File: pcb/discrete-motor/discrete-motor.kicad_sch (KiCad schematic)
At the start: 28 parts, among them J1 ScrewTerminal, U1 PinHeader8, U2 PinHeader8

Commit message: wip
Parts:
- removed CCLFCUR1: (no value), Capacitor_SMD:C_0603_1608Metric, symbol Device:C
- removed RCLFCUR1, RCLPCUR1, RCLSCUR1: (no value), Resistor_SMD:R_0603_1608Metric, symbol Device:R
- removed UCLCUR1: (no value), Package_SO:SOIC-5, symbol Comparator:LMV331
- added CF10, CSA10: 100n, Capacitor_SMD:C_0603_1608Metric, symbol Device:C
- added R10: 10m, Resistor_SMD:R_1206_3216Metric, symbol Device:R
- added RF10: 1k, Resistor_SMD:R_0603_1608Metric, symbol Device:R
- added UA10: (no value), Package_TO_SOT_SMD:SOT-23-6, symbol Amplifier_Current:INA181
- C10: value (none) -> 100n
- J1: value ScrewTerminal -> (none)
- QH10, QL10: footprint Package_TO_SOT_THT:TO-263-2 -> fixme!!!
- R1: value (none) -> 4.7k
- R4: value (none) -> 330
- RH10, RL10: value (none) -> 10
- U1, U2: value PinHeader8 -> (none)
- U3, U4: value ~ -> (none)
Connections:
- net 3V3: now also CSA10.1, UA10.5 (REF)
- net GND: now also CF10.2, CSA10.2, R10.2, UA10.2 (GND), UA10.4 (-), UA10.6 (V+)
- net at U10.3 (~{SD}): now also U1.7 (Pin_7)
- net at U2.2 (Pin_2): now also CF10.1, RF10.2
- net at J4.1 (Pin_1): now also C10.2, QH10.3 (S), QL10.2 (D), U10.6 (VS)
- net at QL10.3 (S): now also R10.1, UA10.3 (+)
- new net: RF10.1, UA10.1
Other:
- moved on the sheet: C10, D10, QH10, QL10, RH10, RL10, U10

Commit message: wip
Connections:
- net at U1.7 (Pin_7): no longer U10.3 (~{SD})
- net at U1.8 (Pin_8): now also U10.3 (~{SD})

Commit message: discrete motor
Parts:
- removed R10: 10m, Resistor_SMD:R_1206_3216Metric, symbol Device:R
- added C11, C12, C13, CF11, CSA11: 100n, Capacitor_SMD:C_0603_1608Metric, symbol Device:C
- added D11, D12, D13: ~, Diode_SMD:D_SMA, symbol Device:D
- added QH11, QH12, QH13, QL11, QL12, QL13: ~, Package_TO_SOT_SMD:TO-263-2, symbol Transistor_FET:Q_NMOS_GDS
- added RF11: 1k, Resistor_SMD:R_0603_1608Metric, symbol Device:R
- added RH11, RH12, RH13, RL11, RL12, RL13: 10, Resistor_SMD:R_0603_1608Metric, symbol Device:R
- added RS10, RS11: 10m, Resistor_SMD:R_1206_3216Metric, symbol Device:R
- added U11, U12, U13: ~, Package_SO:SOIC-8_3.9x4.9mm_P1.27mm, symbol Driver_FET:IR2104
- added UA11: ~, Package_TO_SOT_SMD:SOT-23-6, symbol Amplifier_Current:INA181
- D1, D10, J1, J2, J3, J4, J5, U1, U2, U3, U4, U5, U6, U7, U8, UA10: value (none) -> ~
- QH10, QL10: value (none) -> ~; footprint fixme!!! -> Package_TO_SOT_SMD:TO-263-2; lcsc (none) -> C409762
- U10: value (none) -> ~; footprint Package_SO:SOIC-8 -> Package_SO:SOIC-8_3.9x4.9mm_P1.27mm; lcsc (none) -> C5804631
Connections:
- net 12V: now also D11.2 (A), D12.2 (A), D13.2 (A), QH11.2 (D), QH12.2 (D), QH13.2 (D), U11.1 (VCC), U12.1 (VCC), U13.1 (VCC)
- net 3V3: now also CSA11.1, UA11.5 (REF)
- net GND: now also CF11.2, CSA11.2, RS10.2, RS11.2, U11.4 (COM), U12.4 (COM), U13.4 (COM), UA11.2 (GND), UA11.4 (-), UA11.6 (V+)
- net at U2.1 (Pin_1): no longer U10.2 (IN)
- net at U2.4 (Pin_4): now also CF11.1, RF11.2
- net at J4.2 (Pin_2): now also C11.2, QH11.3 (S), QL11.2 (D), U11.6 (VS)
- net at J4.3 (Pin_3): now also C12.2, QH12.3 (S), QL12.2 (D), U12.6 (VS)
- net at J4.4 (Pin_4): now also C13.2, QH13.3 (S), QL13.2 (D), U13.6 (VS)
- net at QL10.3 (S), UA10.3 (+): now also QL11.3 (S), RS10.1
- net at U1.2 (Pin_2): now also U10.2 (IN)
- net at U1.3 (Pin_3): now also U11.2 (IN)
- net at U1.6 (Pin_6): now also U12.2 (IN)
- net at U1.7 (Pin_7): now also U13.2 (IN)
- net at U1.8 (Pin_8), U10.3 (~{SD}): now also U11.3 (~{SD}), U12.3 (~{SD}), U13.3 (~{SD})
- new net: C12.1, D12.1 (K), U12.8 (VB)
- new net: C13.1, D13.1 (K), U13.8 (VB)
- new net: QL11.1 (G), RL11.2
- new net: C11.1, D11.1 (K), U11.8 (VB)
- new net: QL12.1 (G), RL12.2
- new net: QL12.3 (S), QL13.3 (S), RS11.1, UA11.3 (+)
- new net: RL11.1, U11.5 (LO)
- new net: RH11.1, U11.7 (HO)
- new net: RL13.1, U13.5 (LO)
- new net: RH13.1, U13.7 (HO)
- new net: QH13.1 (G), RH13.2
- new net: RF11.1, UA11.1
- new net: QH11.1 (G), RH11.2
- new net: QL13.1 (G), RL13.2
- new net: QH12.1 (G), RH12.2
- new net: RL12.1, U12.5 (LO)
- new net: RH12.1, U12.7 (HO)

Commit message: pcb wip
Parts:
- C10, C11, C12, C13, CF10, CF11, CSA10, CSA11: lcsc C53084461 -> C1590
- D1, D10, D11, D12, D13, J1, J2, J3, J4, J5, U1, U2, U3, U4, U5, U6, U7, U8, UA10, UA11: value ~ -> (none)
- QH10, QH11, QH12, QH13, QL10, QL11, QL12, QL13: value ~ -> (none); lcscRot (none) -> 180
- RH10, RH11, RH12, RH13, RL10, RL11, RL12, RL13: footprint Resistor_SMD:R_0603_1608Metric -> Resistor_SMD:R_0402_1005Metric
- U10, U11, U12, U13: value ~ -> (none); lcscRot (none) -> -90

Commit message: wip
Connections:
- net 12V: no longer D10.2 (A), D11.2 (A), D12.2 (A), D13.2 (A), QH10.2 (D), QH11.2 (D), QH12.2 (D), QH13.2 (D), U10.1 (VCC), U11.1 (VCC), U12.1 (VCC), U13.1 (VCC)
- net GND: now also J2.1 (Pin_1)
- net VMOT: now reaches J2.2 (Pin_2)
- net VMOT: now also D10.2 (A), D11.2 (A), D12.2 (A), D13.2 (A), QH10.2 (D), QH11.2 (D), QH12.2 (D), QH13.2 (D), U10.1 (VCC), U11.1 (VCC), U12.1 (VCC), U13.1 (VCC)
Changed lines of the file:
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@@
     )
   )
-  (label "12V"
-    (at 76.2 119.38 180)
-    (effects
-      (font
-        (size 1.27 1.27)
-      )
-      (justify right bottom)
-    )
-  )
-  (label "12V"
-    (at 76.2 88.9 180)
-    (effects
-      (font
-        (size 1.27 1.27)
-      )
-      (justify right bottom)
-    )
-  )
   (label "GND"
     (at 76.2 83.82 180)
@@
     )
   )
-  (label "12V"
-    (at 107.95 60.96 180)
-    (effects
-      (font
-        (size 1.27 1.27)
-      )
-      (justify right bottom)
-    )
-  )
   (label "GND"
     (at 123.19 95.25 180)
@@
     )
   )
-  (label "12V"
-    (at 107.95 121.92 180)
-    (effects
-      (font
-        (size 1.27 1.27)
-      )
-      (justify right bottom)
-    )
-  )
   (label "3V3"
     (at 97.79 34.29 180)
@@
     )
   )
-  (label "12V"
-    (at 76.2 58.42 180)
-    (effects
-      (font
-        (size 1.27 1.27)
-      )
-      (justify right bottom)
-    )
-  )
   (label "GND"
     (at 133.35 140.97 180)
@@
     )
   )
-  (label "12V"
-    (at 76.2 149.86 180)
-    (effects
-      (font
-        (size 1.27 1.27)
-      )
-      (justify right bottom)
-    )
-  )
   (label "GND"
     (at 76.2 114.3 180)
@@
     )
   )
-  (label "12V"
-    (at 107.95 91.44 180)
-    (effects
-      (font
-        (size 1.27 1.27)
-      )
-      (justify right bottom)
-    )
-  )
   (label "5V"
     (at 97.79 29.21 180)
@@
     )
   )
-  (label "12V"
-    (at 107.95 152.4 180)
-    (effects
-      (font
-        (size 1.27 1.27)
-      )
-      (justify right bottom)
-    )
-  )
   (label "GND"
     (at 62.23 27.94 180)
@@
     )
   )
+  (label "GND"
+    (at 48.260000000000005 49.53 180)
+    (effects
+      (font
+        (size 1.27 1.27)
+      )
+      (justify right bottom)
+    )
+  )
+  (label "VMOT"
+    (at 48.260000000000005 52.07 180)
+    (effects
+      (font
+        (size 1.27 1.27)
+      )
+      (justify right bottom)
+    )
+  )
+  (label "VMOT"
+    (at 76.2 58.42 180)
+    (effects
+      (font
+        (size 1.27 1.27)
+      )
+      (justify right bottom)
+    )
+  )
+  (label "VMOT"
+    (at 107.95 60.96000000000001 180)
+    (effects
+      (font
+        (size 1.27 1.27)
+      )
+      (justify right bottom)
+    )
+  )
+  (label "VMOT"
+    (at 76.2 88.89999999999999 180)
+    (effects
+      (font
+        (size 1.27 1.27)
+      )
+      (justify right bottom)
+    )
+  )
+  (label "VMOT"
+    (at 107.95 91.44 180)
+    (effects
+      (font
+        (size 1.27 1.27)
+      )
+      (justify right bottom)
+    )
+  )
+  (label "VMOT"
+    (at 76.2 119.38000000000001 180)
+    (effects
+      (font
+        (size 1.27 1.27)
+      )
+      (justify right bottom)
+    )
+  )
+  (label "VMOT"
+    (at 107.95 121.92 180)
+    (effects
+      (font
+        (size 1.27 1.27)
+      )
+      (justify right bottom)
+    )
+  )
+  (label "VMOT"
+    (at 76.2 149.86 180)
+    (effects
+      (font
+        (size 1.27 1.27)
+      )
+      (justify right bottom)
+    )
+  )
+  (label "VMOT"
+    (at 107.95 152.39999999999998 180)
+    (effects
+      (font
+        (size 1.27 1.27)
+      )
+      (justify right bottom)
+    )
+  )

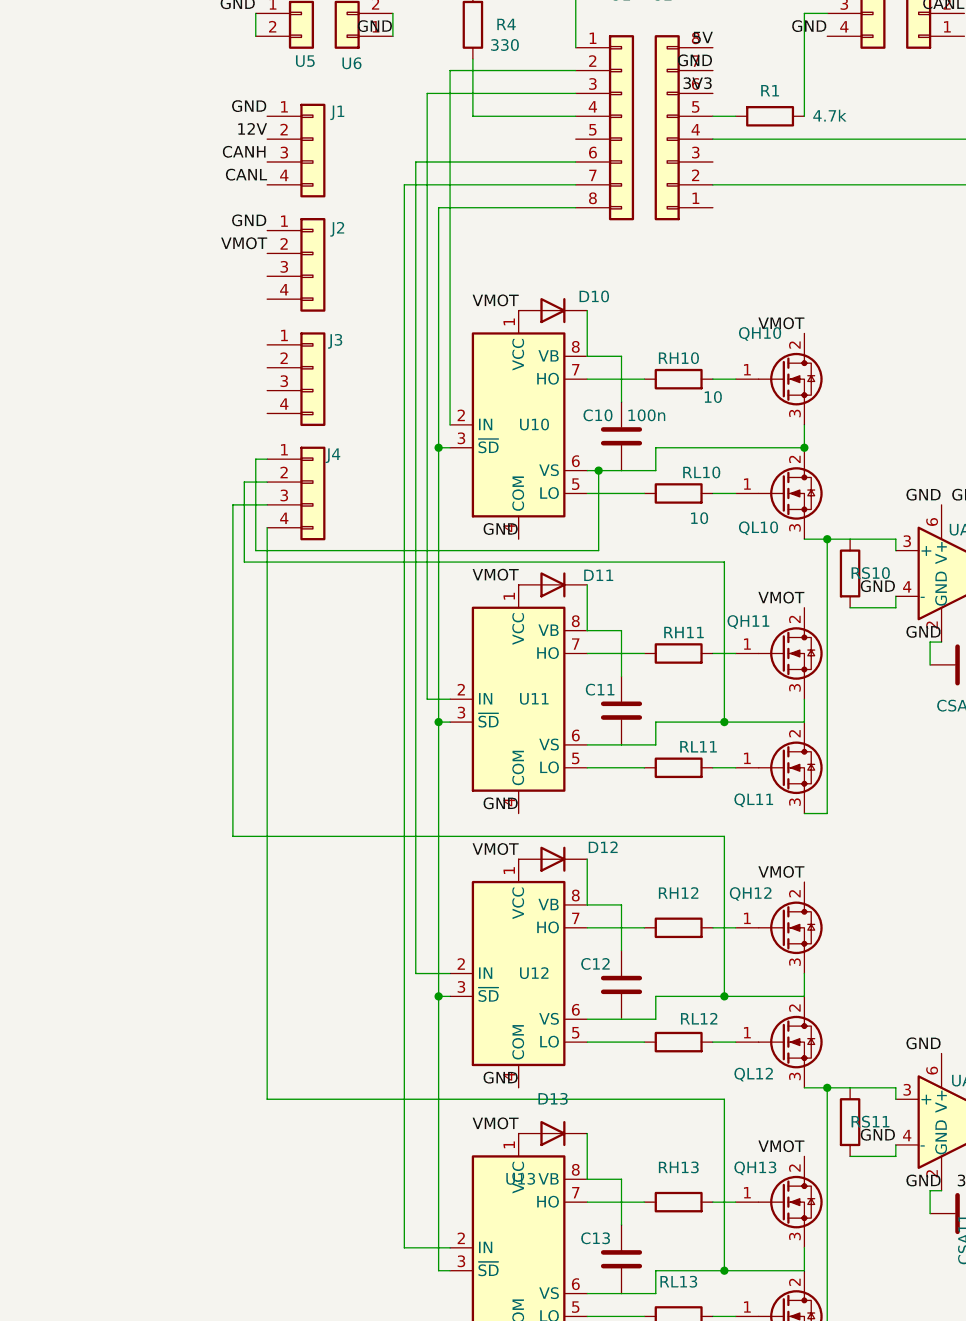
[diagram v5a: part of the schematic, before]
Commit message: discrete motor fixes
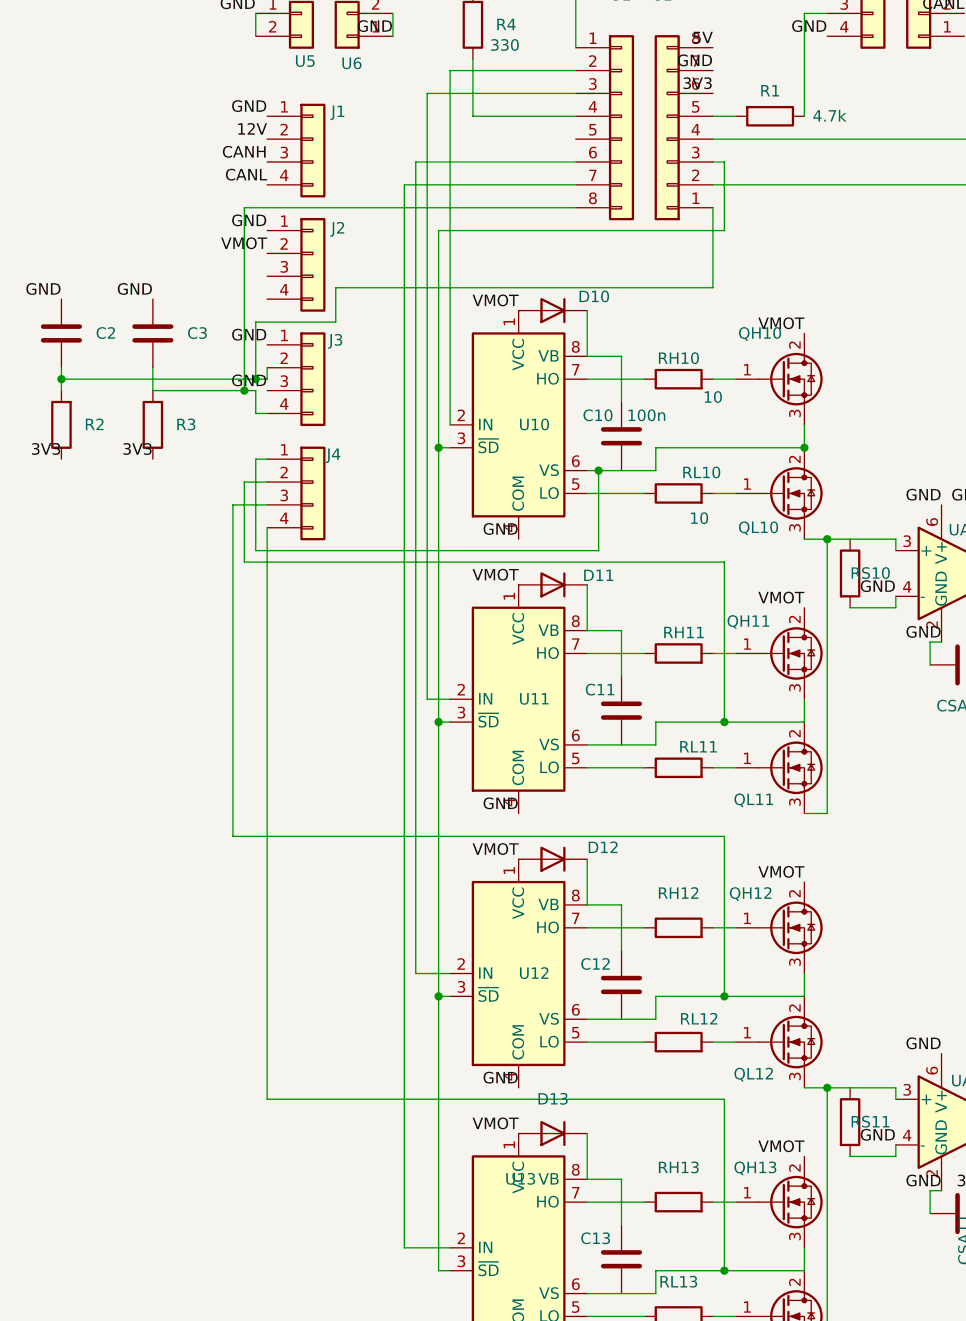
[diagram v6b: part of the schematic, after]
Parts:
- added C2, C3: 100n, Capacitor_SMD:C_0603_1608Metric, symbol Device:C
- added R2, R3: 4.7k, Resistor_SMD:R_0603_1608Metric, symbol Device:R
- RH10, RH11, RH12, RH13, RL10, RL11, RL12, RL13: footprint Resistor_SMD:R_0402_1005Metric -> Resistor_SMD:R_0603_1608Metric; lcsc C174147 -> C22859
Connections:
- net 3V3: now also R2.1, R3.1
- net GND: now also J3.1 (Pin_1), J3.3 (Pin_3), C2.2, C3.2
- net at U2.1 (Pin_1): now also J3.2 (Pin_2), C2.1, R2.2
- net at U2.3 (Pin_3): now also U10.3 (~{SD}), U11.3 (~{SD}), U12.3 (~{SD}), U13.3 (~{SD})
- net at J3.4 (Pin_4): now also U1.8 (Pin_8), C3.1, R3.2
